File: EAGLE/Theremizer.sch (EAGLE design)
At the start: 135 parts, among them IC1 AS3320, IC2 NE5532D, IC3 TL072D, IC4 NE5532D, J1 3x2 M, J2 1x6 M, J3 AUDIO_JACK_TRS_0.25"_PTH_RA, J4 POWER_JACK, J5 AUDIO_JACK_TRS_0.25"_PTH_RA, Q1 PMV45EN2R, Q2 J310, Q3 J310, Q4 J310, Q6 2N5088, Q7 2N5088, SW1 !RESET, U1 NCP1117ST50T3G, U2 MCU-ATMEGA328P-AU(TQFP32), U3 DCWN03B-15, U4 LTC2645CMS-L8PBF, X1 16 MHz

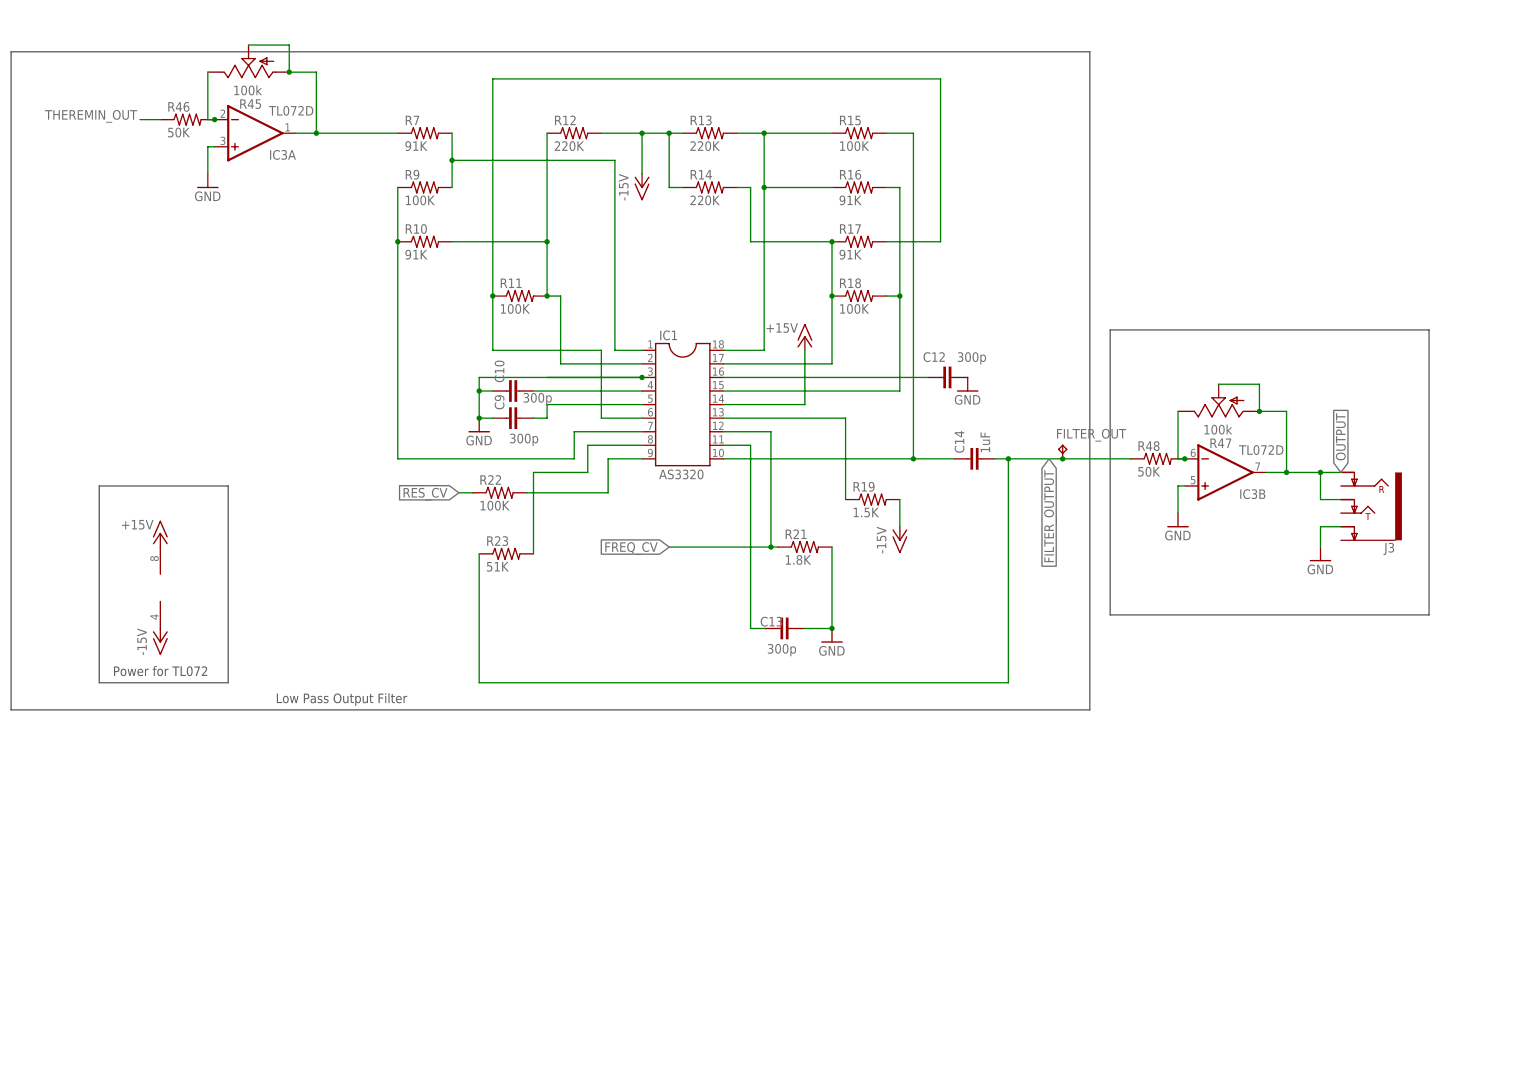
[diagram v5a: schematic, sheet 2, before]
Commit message: Changed cap values for mixer output, added decoupling caps, 9V regulator
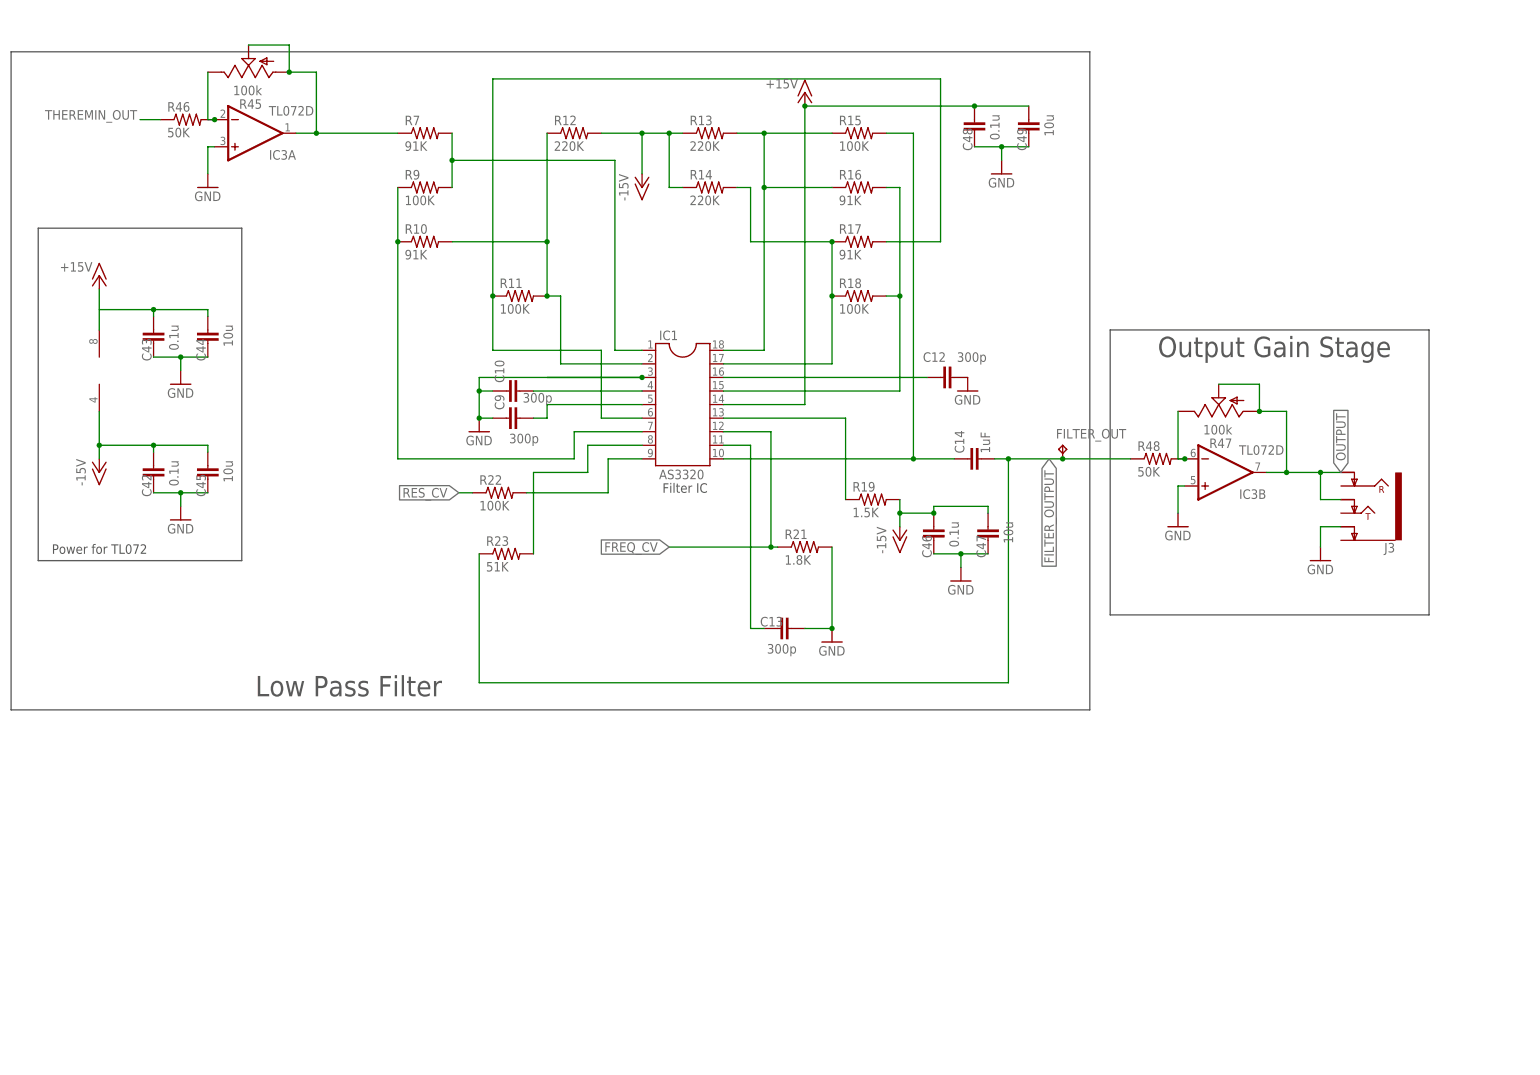
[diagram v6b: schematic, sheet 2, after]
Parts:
- removed $U1: SA602AD, SA602AN:SA602AD
- added C42, C43, C46, C48, C51: 0.1u, rcl:C-EUC0805
- added C44, C45, C47, C49: 10u, rcl:C-EUC0805
- added C50: 0.33u, rcl:C-EUC0805
- added R51: 1M, rcl:R-US_R0805
- added U5: (no value), SA602AN:SA602AD
- added U6: UA78M09, uA78Mx:µA78MX
- C2: value 100n -> 0.1u
- C40: value 10n -> 1n
- C41: value 10n -> 47n
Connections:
- new net -15V1: C43.2, C44.2
- new net N$59: R51.1, U5.OUTB
- net +15V: now also C48.2, C49.2
- net +9V: now also C51.1, U5.VCC, U6.OUT; no longer $U1.VCC
- net -15V: now also C42.2, C45.2, C46.2, C47.2
- net GND: now also C42.1, C43.1, C44.1, C45.1, C46.1, C47.1, C48.1, C49.1, C50.2, C51.2, R51.2, U5.GND, U5.OSCB, U5.OSCE, U6.GND; no longer $U1.GND, $U1.OSCB, $U1.OSCE, $U1.OUTB
- net N$24: now also U5.INA; no longer $U1.INA
- net N$36: now also U5.INB; no longer $U1.INB
- net N$51: now also C50.1, U6.IN
- net THEREMIN_OUT: now also U5.OUTA; no longer $U1.OUTA
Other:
- note added: "Filter IC"
- note added: "Low Pass Filter"
- note added: "Output Gain Stage"
- note removed: "Low Pass Output Filter"

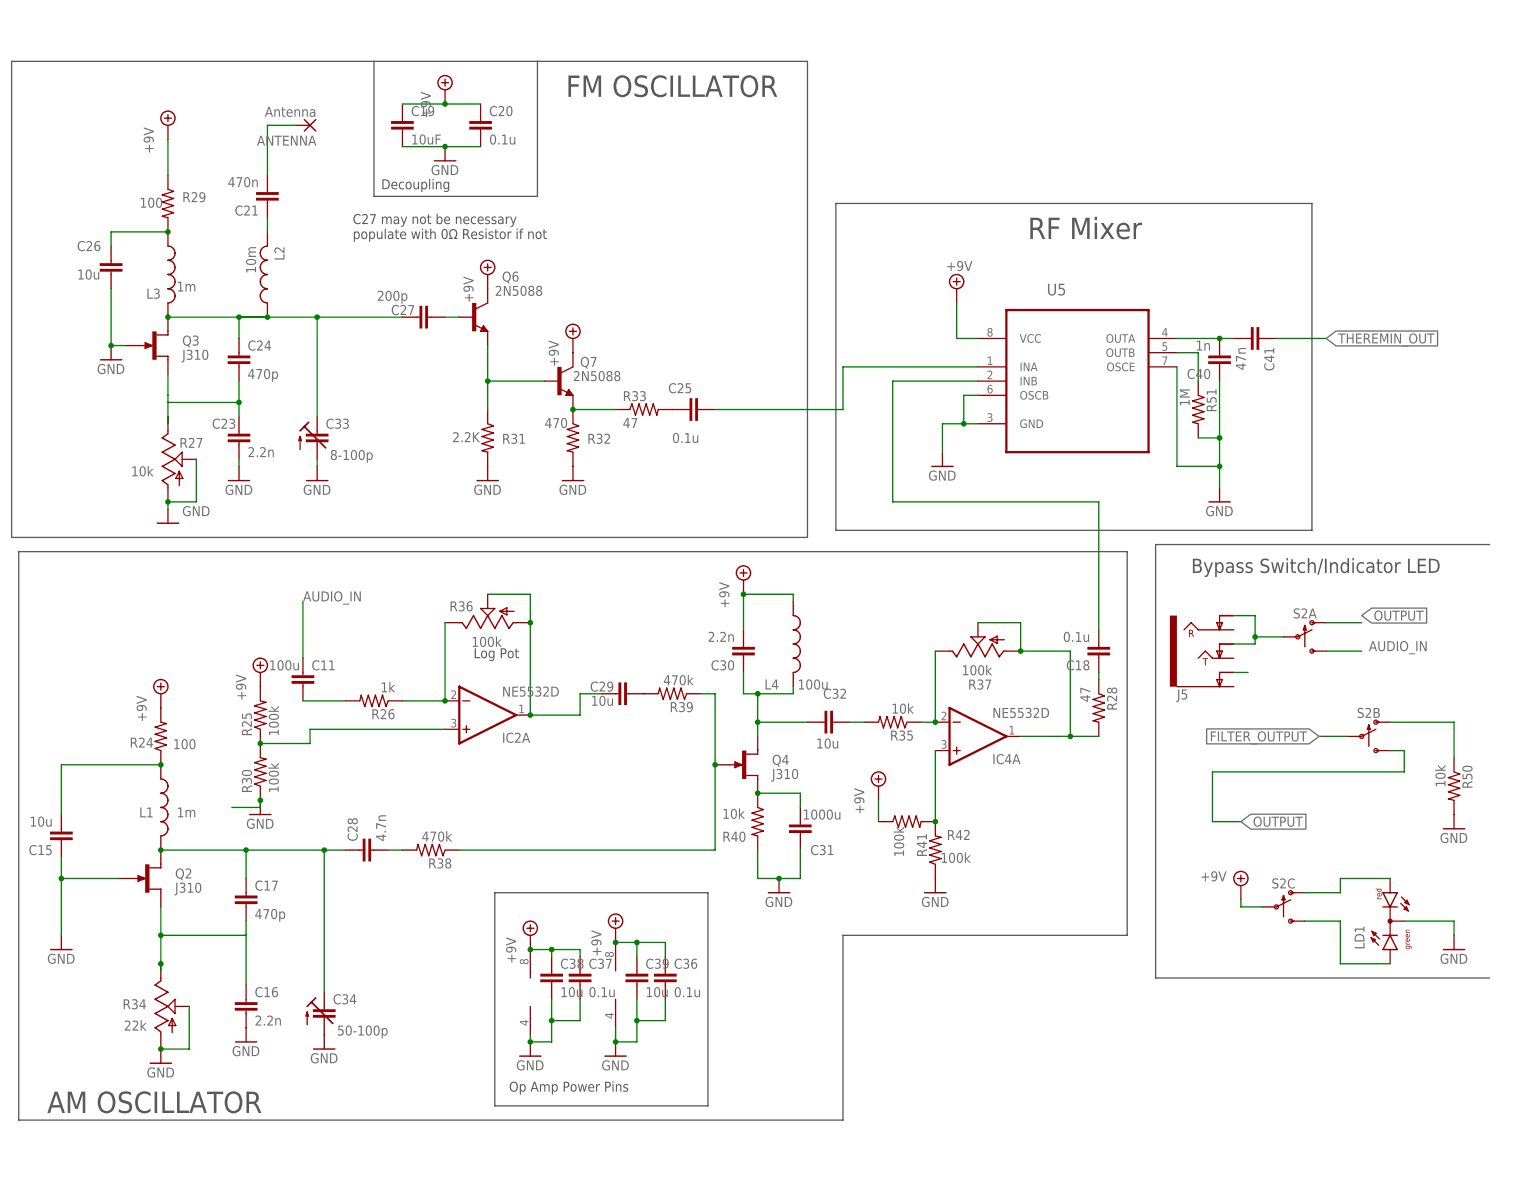
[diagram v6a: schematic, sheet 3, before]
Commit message: Added decoupling caps and analog CV
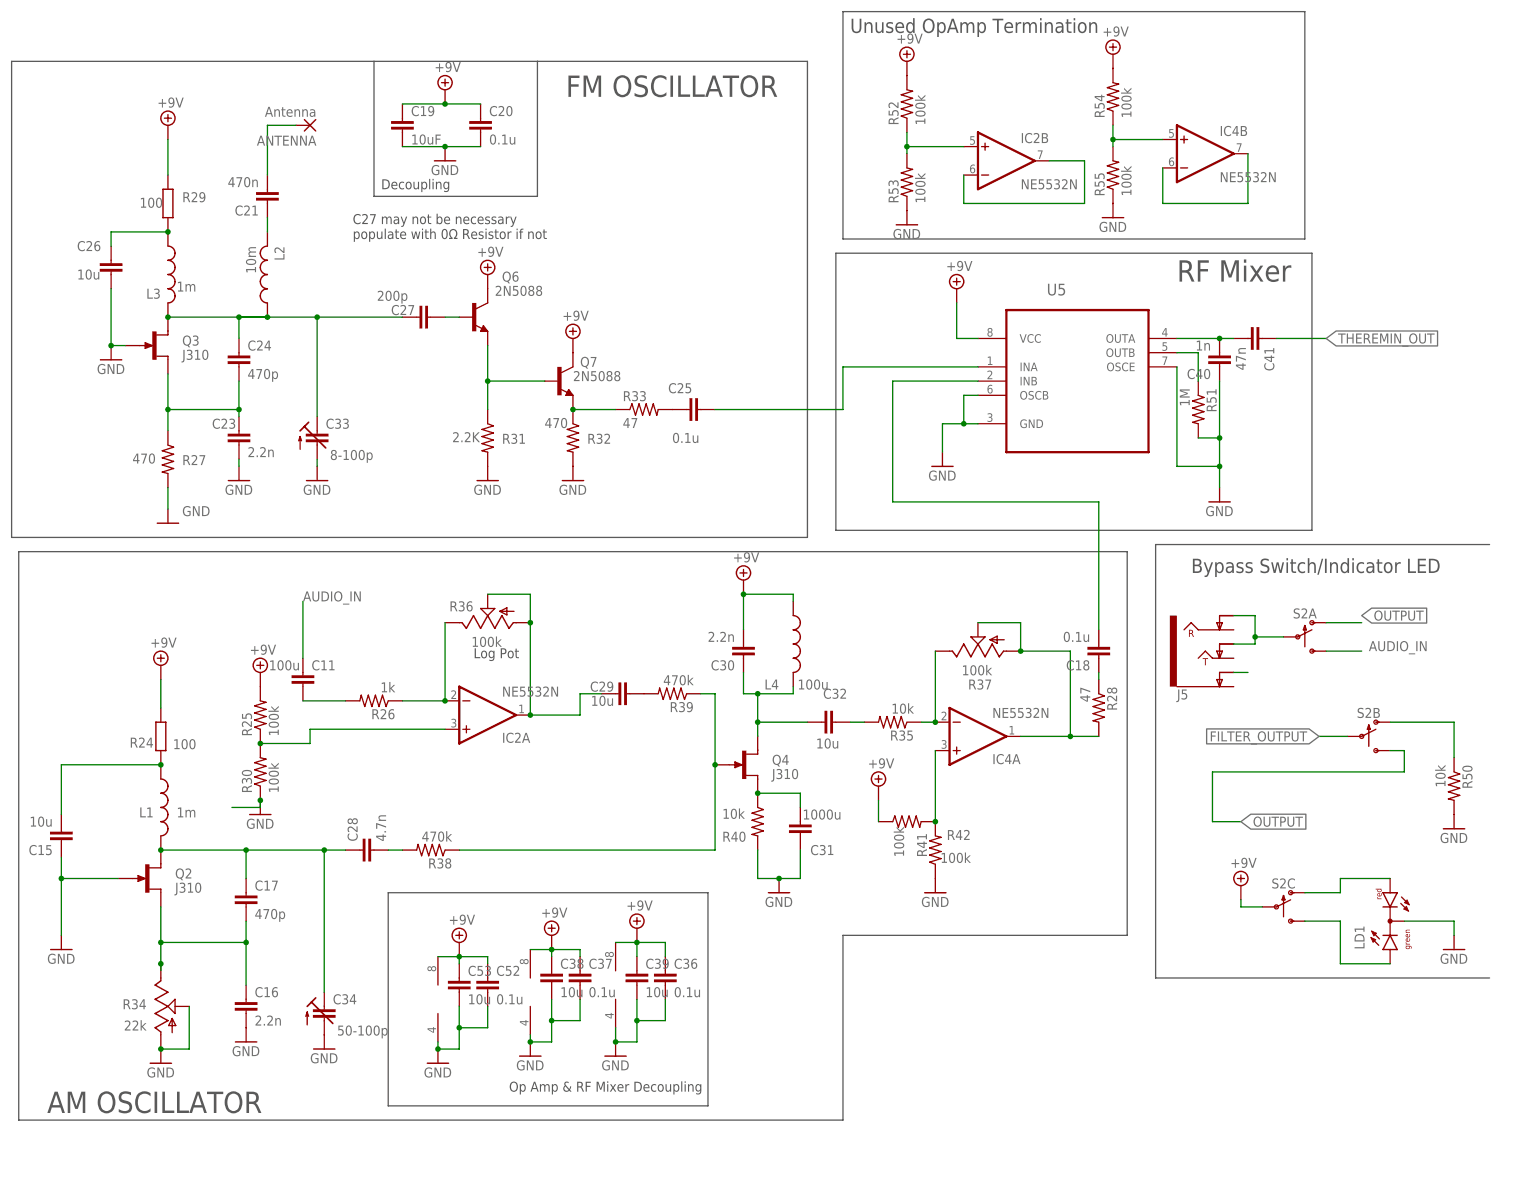
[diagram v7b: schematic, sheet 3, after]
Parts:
- added C52: 0.1u, rcl:C-EUC0805
- added C53: 10u, rcl:C-EUC0805
- added IC5: NE5532N, linear:NE5532N
- added R52, R53, R54, R55: 100k, rcl:R-US_R0805
- added R56, R58: 51K, rcl:R-US_R0805
- added R57, R59: 100k, pot:TRIM_US-ECP10P
- IC2, IC4: value NE5532D -> NE5532N; device linear:NE5532D -> linear:NE5532N
- R24, R29: device rcl:R-US_R0805 -> rcl:R-EU_PRL1632
- R27: value 10k -> 470; device pot:TRIM_US-PT10 -> rcl:R-US_R0805
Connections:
- removed net -15V1: C43.2, C44.2
- new net N$60: IC2B.-IN, IC2B.OUT
- new net N$61: IC2B.+IN, R52.1, R53.2
- new net N$62: IC4B.+IN, R54.1, R55.2
- new net N$63: IC4B.-IN, IC4B.OUT
- new net N$64: C23.1, C24.2, Q3.S, R27.1
- new net N$65: R58.1, R59.E
- net +15V: now also C43.2, C44.2; no longer C19.1, C20.1, C30.2, C36.1, C37.1, C38.1, C39.1, IC2P.V+, IC4P.V+, L4.1, Q6.C, Q7.C, R24.2, R25.2, R29.1, R41.1
- net +5V: now also R56.2, R58.2
- net +9V: now also C19.1, C20.1, C30.2, C36.1, C37.1, C38.1, C39.1, C52.1, C53.1, IC2P.V+, IC4P.V+, IC5P.V+, L4.1, Q6.C, Q7.C, R24.2, R25.2, R29.1, R41.1, R52.2, R54.2
- net FREQ_CV: now also R57.S
- net GND: now also C52.2, C53.2, IC5P.V-, R27.2, R53.1, R55.1, R57.A, R59.A; no longer R27.A, R27.S
- net N$32: now also R56.1, R57.E; no longer C23.1, C24.2, Q3.S, R27.E
- net RES_CV: now also R59.S
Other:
- note added: "Analog Control Voltage"
- note added: "Op Amp & RF Mixer Decoupling"
- note added: "Unused OpAmp Termination"
- note removed: "Op Amp Power Pins"
- moved on the sheet: IC3A, R45, R46

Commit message: Last BOM
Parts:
- removed C33: 8-100p, rcl:C-TRIMM808
- removed C34: 50-100p, rcl:C-TRIMM808
- removed C52: 0.1u, rcl:C-EUC0805
- removed C53: 10u, rcl:C-EUC0805
- removed IC5: NE5532N, linear:NE5532N
- added JP1, JP2, JP3, JP4, JP5, JP6, JP7, JP8, JP9: (no value), jumper:JP1E
- added PAD1, PAD2, PAD3: (no value), wirepad:2,15/1,0
- added R60: 470, rcl:R-US_R0805
- C11: value 100u -> 10u; device rcl:C-EUC0805 -> rcl:C-US050-025X075
- C14: value 1uF -> 1u
- C15, C26: device rcl:C-EUC0805 -> rcl:C-US050-025X075
- C19: value 10uF -> 10u
- C22, C35: value .1u -> 0.1u
- C28: value 4.7n -> 0.1u
- C29: value 10u -> 0.1u
- C31: value 1000u -> 470p
- C4, C6: value 100n -> 0.1u
- R1, R6: value 10K -> 10k
- R11, R15, R18, R22, R9: value 100K -> 100k
- R2, R3, R4, R5: value 1K -> 1k
- R40: value 10k -> 470
- R56, R58: value 51K -> 274k
- R57, R59: value 100k -> 10k
- U5: value (none) -> SA602AD
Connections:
- new net N$66: JP1.1, PAD2.P
- new net N$67: JP2.2, PAD3.P
- new net N$69: C27.1, JP3.2
- new net N$70: C25.2, JP4.1
- new net N$71: C29.1, JP5.2
- new net N$72: C28.1, JP6.2
- new net N$73: C32.2, JP7.2
- new net N$74: C18.2, JP8.2
- new net N$75: C41.1, JP9.1
- new net N$76: LD1.C, R60.1
- net +9V: no longer C52.1, C53.1, IC5P.V+
- net GND: now also C15.2, JP1.2, JP2.1, R60.2; no longer C15.1, C33.A, C34.A, C52.2, C53.2, IC5P.V-, LD1.C
- net N$22: now also C15.1; no longer C15.2
- net N$24: now also JP4.2; no longer C25.2
- net N$26: now also JP3.1; no longer C27.1, C33.E
- net N$35: now also JP6.1, PAD1.P; no longer C28.1, C34.E
- net N$36: now also JP8.1; no longer C18.2
- net N$41: now also JP5.1; no longer C29.1
- net N$45: now also JP7.1; no longer C32.2
- net THEREMIN_OUT: now also JP9.2; no longer C41.1
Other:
- note added: "0"
- note added: "5V Regulator"
- note added: "9V Regulator"
- note added: "ATMega328p/Power Supply/DAC"
- note added: "Lowpass Filter/Output Gain Stage"
- note added: "Oscillators/RF Mixer"
- note added: "THZ-100"
- note added: "Variable Cap 2-200pF Panel Mount"
- note added: "±15V Regulator"
- note removed: "1"
- moved on the sheet: C15, C28, C36, C37, C38, C39, R2, R38
